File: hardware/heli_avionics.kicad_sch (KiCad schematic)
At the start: 15 parts, among them J1 UPDI, J7 Conn_01x02, SW1 Reset, U1 ATmega4808-A

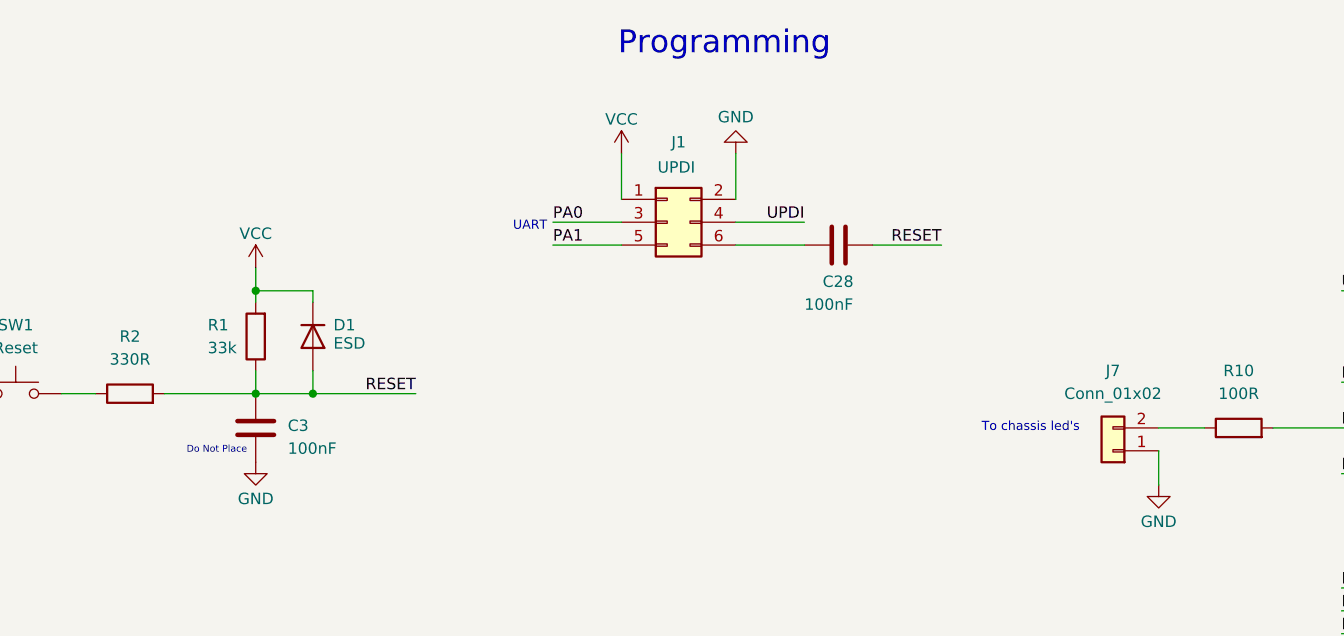
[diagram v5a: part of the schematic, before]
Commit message: Assigned footprints for connectors
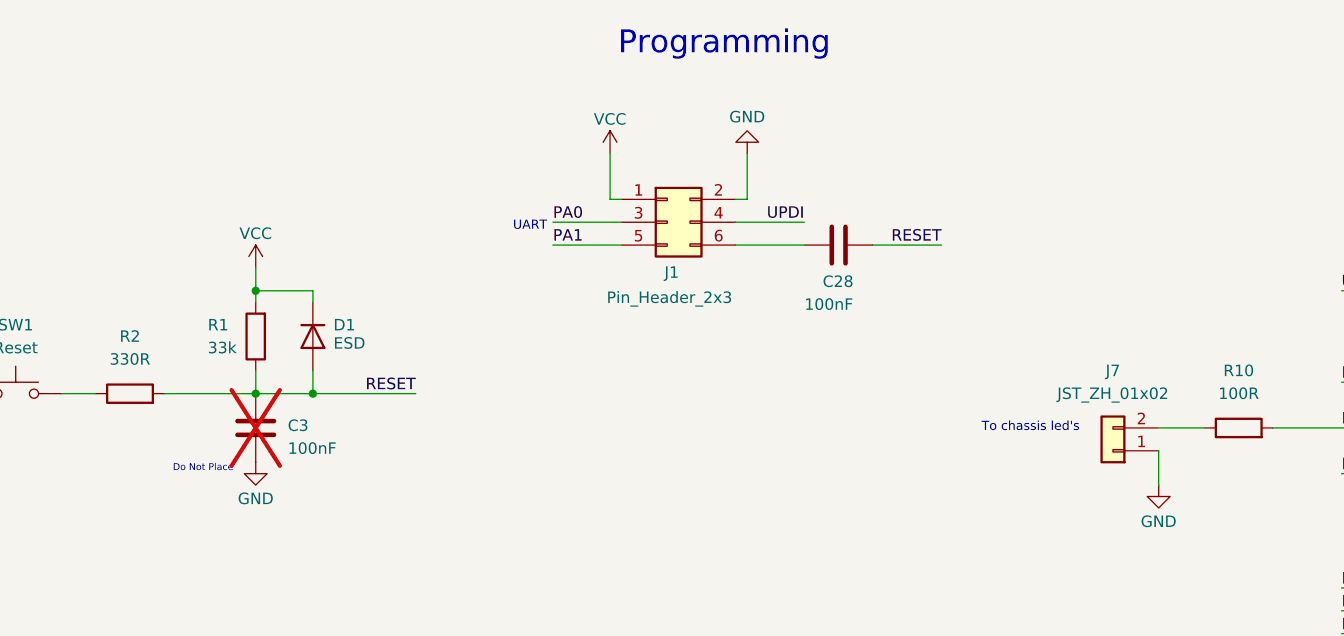
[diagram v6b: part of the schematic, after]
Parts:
- C3: now not fitted
- J1: value UPDI -> Pin_Header_2x3; footprint (none) -> Connector_PinHeader_2.54mm:PinHeader_2x03_P2.54mm_Vertical
- J7: value Conn_01x02 -> JST_ZH_01x02; footprint (none) -> Connector_JST:JST_ZH_B2B-ZR_1x02_P1.50mm_Vertical
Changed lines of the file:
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@@
+	(wire
+		(pts
+			(xy 100.33 43.18) (xy 101.6 43.18)
+		)
+		(stroke
+			(width 0)
+			(type default)
+		)
+	)
 	(wire
 		(pts
@@
 	(wire
 		(pts
+			(xy 115.57 43.18) (xy 114.3 43.18)
+		)
+		(stroke
+			(width 0)
+			(type default)
+		)
+	)
+	(wire
+		(pts
 			(xy 39.37 64.77) (xy 43.18 64.77)
 		)
@@
 	(wire
 		(pts
-			(xy 101.6 38.1) (xy 101.6 43.18)
+			(xy 100.33 38.1) (xy 100.33 43.18)
 		)
 		(stroke
@@
 	(wire
 		(pts
-			(xy 114.3 38.1) (xy 114.3 43.18)
+			(xy 115.57 38.1) (xy 115.57 43.18)
 		)
 		(stroke
@@
 	(text "Do Not Place"
 		(exclude_from_sim no)
-		(at 56.642 71.12 0)
+		(at 55.118 73.152 0)
 		(effects
 			(font
@@
 			)
 		)
-		(property "Value" "Conn_01x02"
+		(property "Value" "JST_ZH_01x02"
 			(at 156.21 64.77 0)
 			(effects
@@
 			)
 		)
-		(property "Footprint" ""
+		(property "Footprint" "Connector_JST:JST_ZH_B2B-ZR_1x02_P1.50mm_Vertical"
 			(at 156.21 71.12 0)
 			(effects
@@
 	(symbol
 		(lib_id "power:VCC")
-		(at 101.6 38.1 0)
+		(at 100.33 38.1 0)
 		(mirror y)
 		(unit 1)
@@
 		(dnp no)
 		(property "Reference" "#PWR09"
-			(at 101.6 41.91 0)
+			(at 100.33 41.91 0)
 			(effects
 				(font
@@
 		)
 		(property "Value" "VCC"
-			(at 101.6 34.29 0)
+			(at 100.33 34.29 0)
 			(effects
 				(font
@@
 		)
 		(property "Footprint" ""
-			(at 101.6 38.1 0)
+			(at 100.33 38.1 0)
 			(effects
 				(font
@@
 		)
 		(property "Datasheet" ""
-			(at 101.6 38.1 0)
+			(at 100.33 38.1 0)
 			(effects
 				(font
@@
 		)
 		(property "Description" "Power symbol creates a global label with name \"VCC\""
-			(at 101.6 38.1 0)
+			(at 100.33 38.1 0)
 			(effects
 				(font
@@
 		(in_bom yes)
 		(on_board yes)
-		(dnp no)
+		(dnp yes)
 		(property "Reference" "C3"
 			(at 64.516 68.326 0)
@@
 	(symbol
 		(lib_id "power:GND")
-		(at 114.3 38.1 0)
+		(at 115.57 38.1 0)
 		(mirror x)
 		(unit 1)
@@
 		(dnp no)
 		(property "Reference" "#PWR08"
-			(at 114.3 31.75 0)
+			(at 115.57 31.75 0)
 			(effects
 				(font
@@
 		)
 		(property "Value" "GND"
-			(at 114.3 34.036 0)
+			(at 115.57 34.036 0)
 			(effects
 				(font
@@
 		)
 		(property "Footprint" ""
-			(at 114.3 38.1 0)
+			(at 115.57 38.1 0)
 			(effects
 				(font
@@
 		)
 		(property "Datasheet" ""
-			(at 114.3 38.1 0)
+			(at 115.57 38.1 0)
 			(effects
 				(font
@@
 		)
 		(property "Description" "Power symbol creates a global label with name \"GND\" , ground"
-			(at 114.3 38.1 0)
+			(at 115.57 38.1 0)
 			(effects
 				(font
@@
 		(dnp no)
 		(property "Reference" "J1"
-			(at 107.95 36.83 0)
-			(effects
-				(font
-					(size 1.27 1.27)
-				)
-			)
-		)
-		(property "Value" "UPDI"
-			(at 107.696 39.624 0)
-			(effects
-				(font
-					(size 1.27 1.27)
-				)
-			)
-		)
-		(property "Footprint" ""
+			(at 107.188 51.308 0)
+			(effects
+				(font
+					(size 1.27 1.27)
+				)
+			)
+		)
+		(property "Value" "Pin_Header_2x3"
+			(at 106.934 54.102 0)
+			(effects
+				(font
+					(size 1.27 1.27)
+				)
+			)
+		)
+		(property "Footprint" "Connector_PinHeader_2.54mm:PinHeader_2x03_P2.54mm_Vertical"
 			(at 106.68 45.72 0)
 			(effects

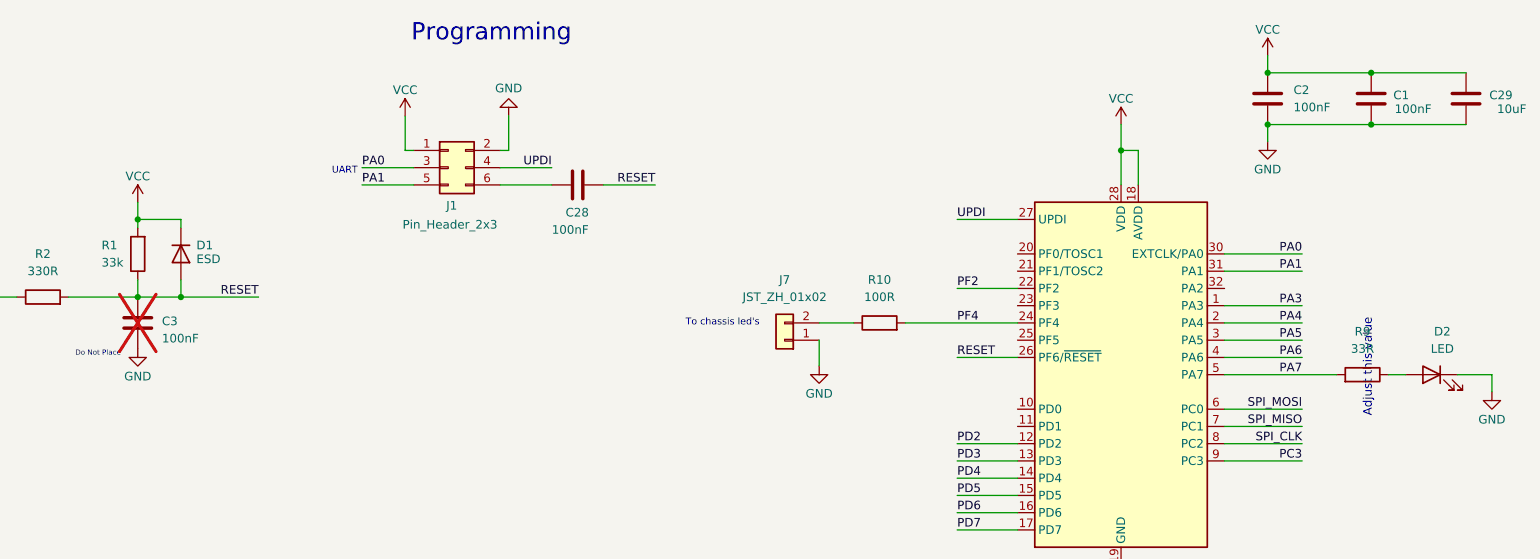
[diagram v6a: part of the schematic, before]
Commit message: Misc small
Remove ESD diode
Add resistor to UPDI line
Fix LED resistor
Assign LED footprint
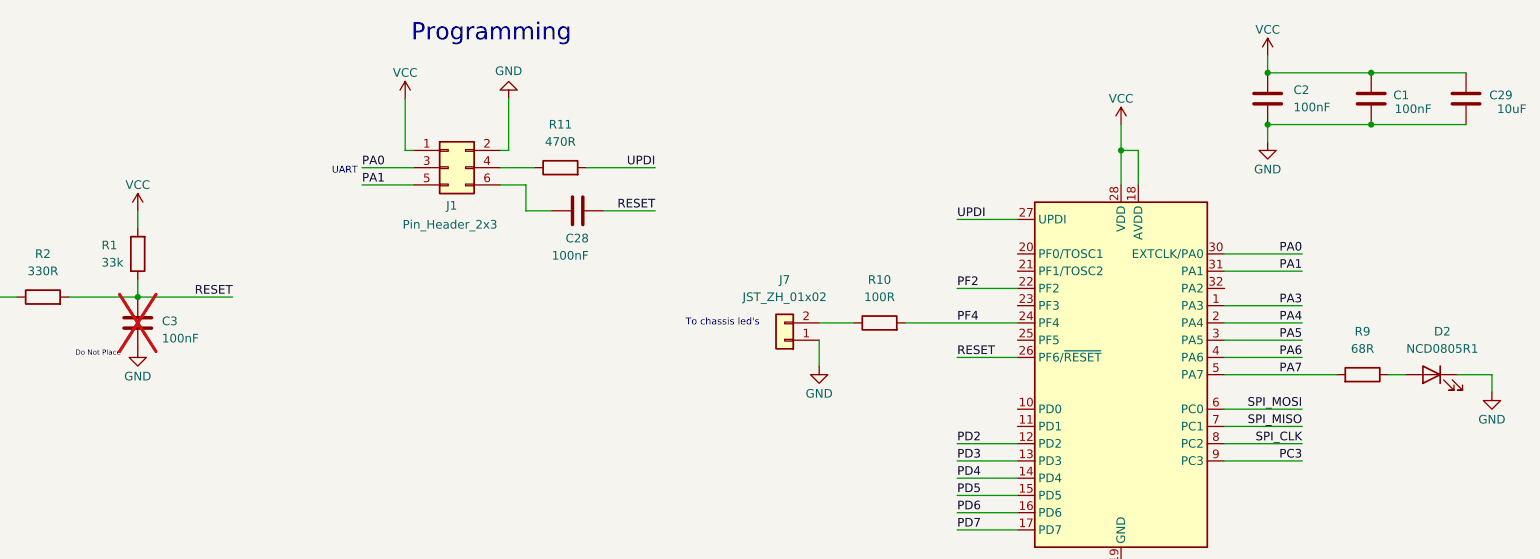
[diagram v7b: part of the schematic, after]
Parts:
- removed D1: ESD, symbol Device:D
- added R11: 470R, symbol Device:R
- D2: value LED -> NCD0805R1; footprint (none) -> LED_SMD:LED_0805_2012Metric_Pad1.15x1.40mm_HandSolder; Color (none) -> Red
- R9: value 33R -> 68R
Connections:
- net UPDI: now also R11.2; no longer J1.4 (Pin_4)
- new net: J1.4 (Pin_4), R11.1
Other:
- note removed: "Adjust this value"
- moved on the sheet: C28

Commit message: Assigned footprint for crystal and button, fixed gitignore
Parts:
- SW1: footprint (none) -> Button_Switch_SMD:SW_Push_SPST_NO_Alps_SKRK
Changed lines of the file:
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@@
 			)
 		)
-		(property "Footprint" ""
+		(property "Footprint" "Button_Switch_SMD:SW_Push_SPST_NO_Alps_SKRK"
 			(at 34.29 59.69 0)
 			(effects
